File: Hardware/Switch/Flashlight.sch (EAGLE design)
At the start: 13 parts

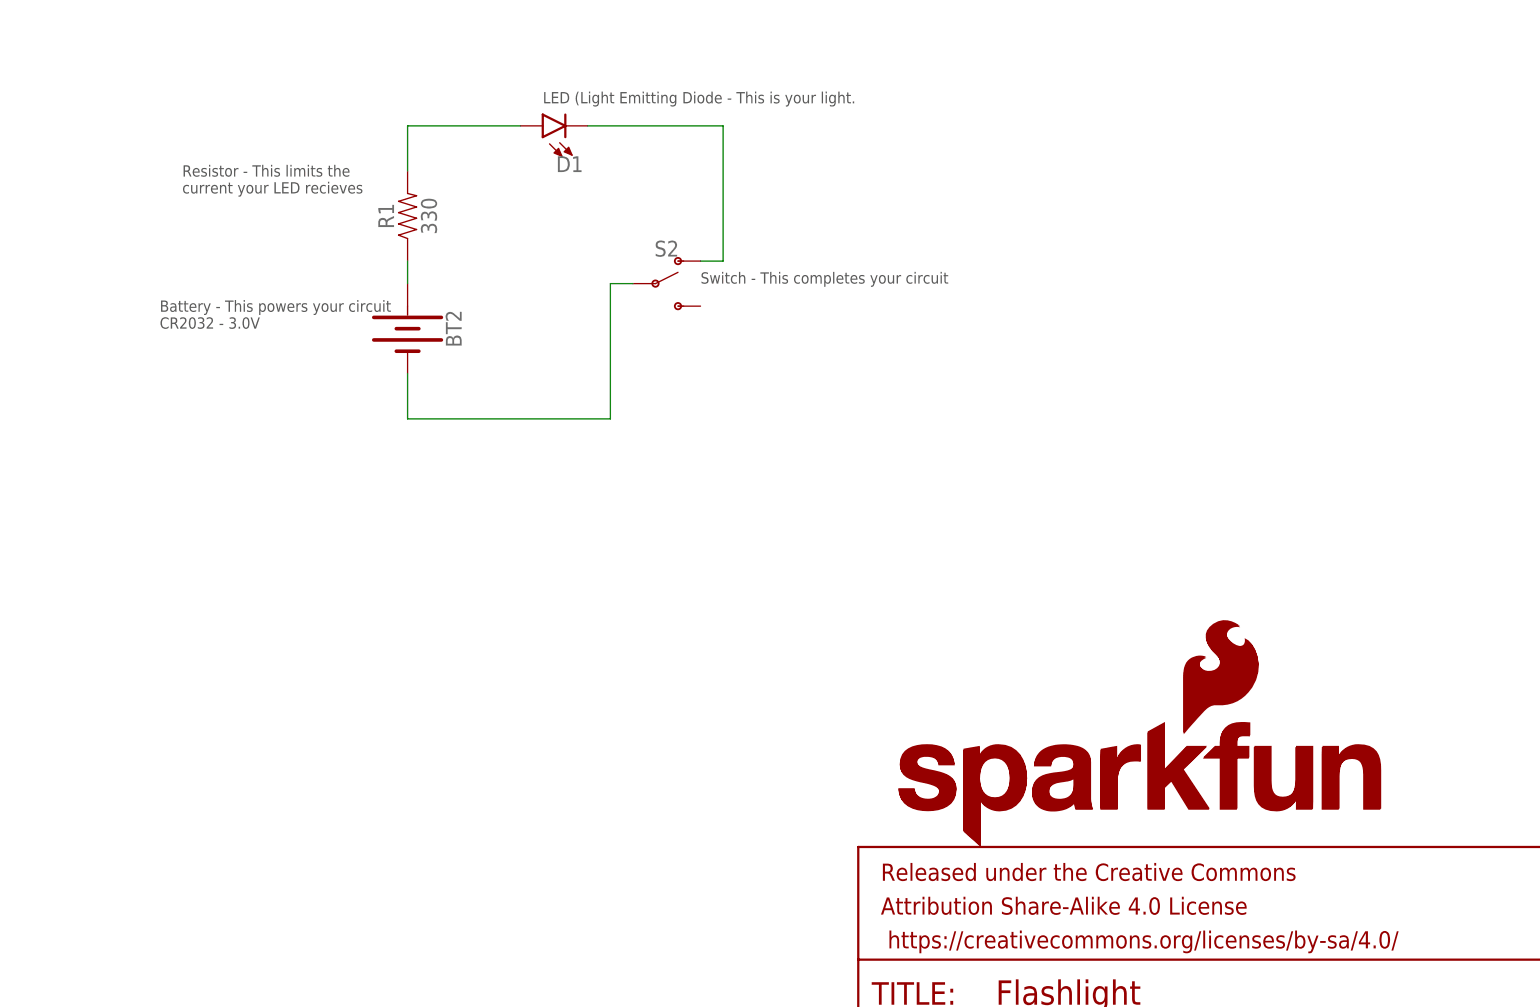
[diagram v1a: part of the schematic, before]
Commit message: Reds
Updated silk to be cleaner, updated version number
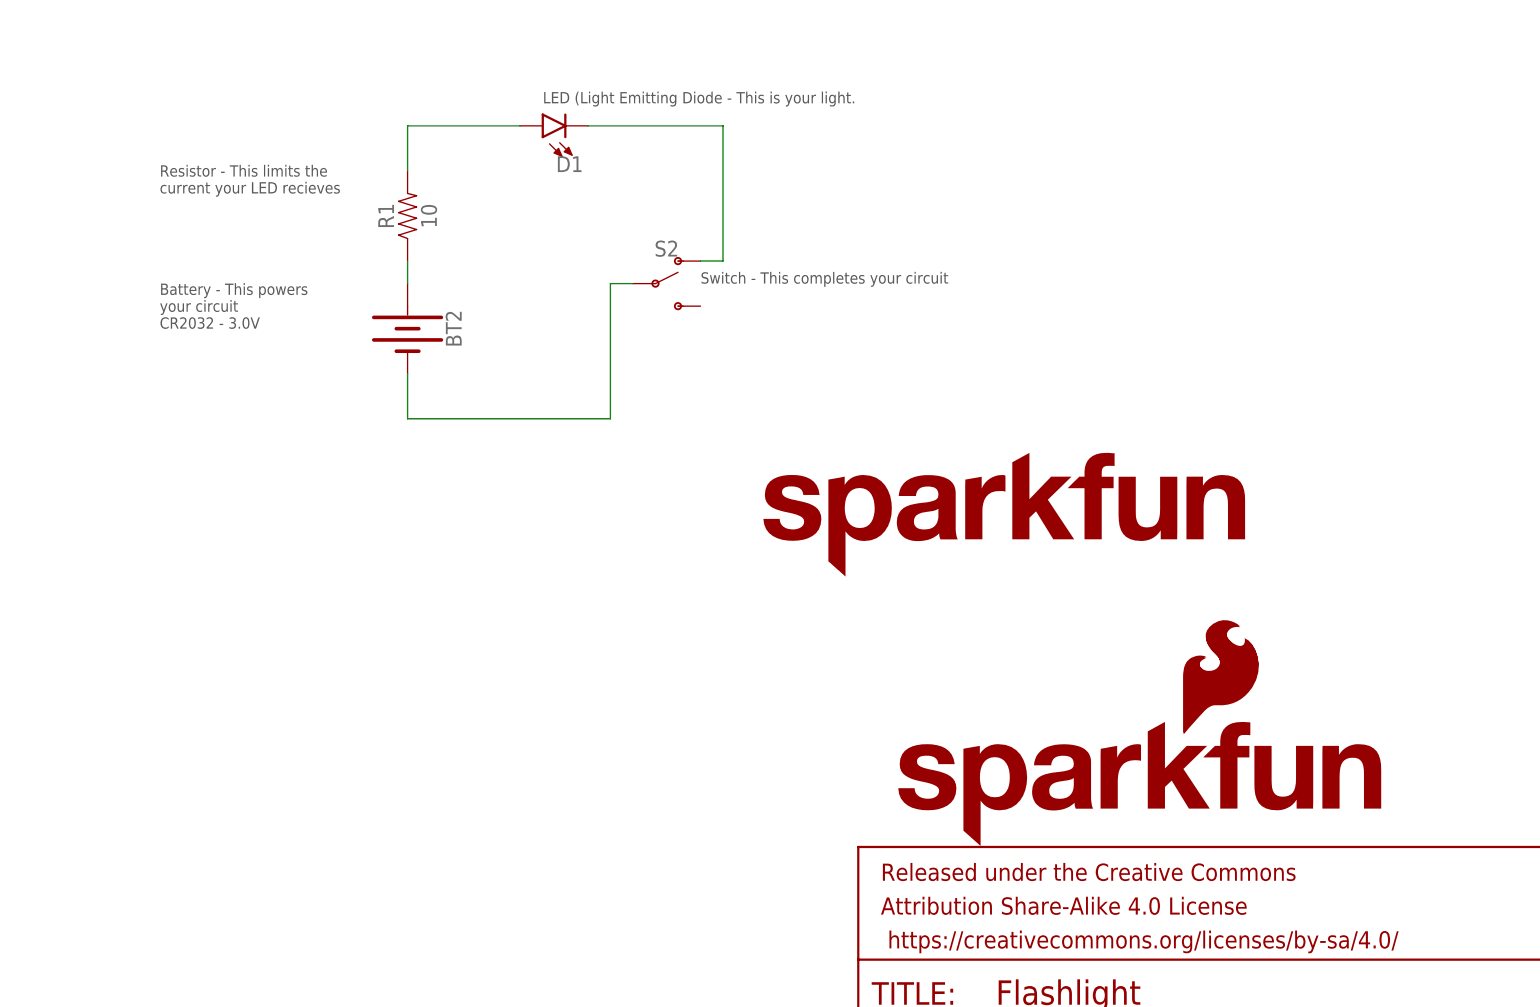
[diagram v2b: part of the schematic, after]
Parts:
- LOGO4: value SFE_LOGO_NAME.1_INCH -> SFE_LOGO_NAME.2_INCH; device SparkFun-Aesthetics:SFE_LOGO_NAME.1_INCH -> SparkFun-Aesthetics:SFE_LOGO_NAME.2_INCH
- R1: value 330 -> 10
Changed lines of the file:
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@@
 <attribute name="PROD_ID" value="9903"/>
 </part>
-<part name="R1" library="SparkFun-Resistors" deviceset="RESISTOR" device="AXIAL-0.3-KIT" value="330">
+<part name="R1" library="SparkFun-Resistors" deviceset="RESISTOR" device="AXIAL-0.3-KIT" value="10">
 <attribute name="PROD_ID" value="8371"/>
 </part>
@@
 <part name="H2" library="SparkFun-Hardware" deviceset="STAND-OFF" device=""/>
 <part name="S2" library="SparkFun-Switches" deviceset="SWITCH-SPDT" device="-PTH-11.6X4.0MM-KIT"/>
-<part name="LOGO4" library="SparkFun-Aesthetics" deviceset="SFE_LOGO_NAME" device=".1_INCH"/>
 <part name="LOGO3" library="SparkFun-Aesthetics" deviceset="SFE_LOGO_NAME_FLAME" device=".2_INCH"/>
 <part name="BT2" library="SparkFun-Batteries" deviceset="BATTERY" device="-20MM_PTH_KIT">
@@
 <part name="H3" library="SparkFun-Hardware" deviceset="STAND-OFF" device=""/>
 <part name="H4" library="SparkFun-Hardware" deviceset="STAND-OFF" device=""/>
+<part name="LOGO4" library="SparkFun-Aesthetics" deviceset="SFE_LOGO_NAME" device=".2_INCH"/>
 </parts>
 <sheets>
@@
 <text x="167.64" y="7.62" size="3.81" layer="94">Michelle Shorter</text>
 <text x="43.18" y="134.62" size="5.08" layer="97" font="vector">SparkFun Flashlight Soldering Kit</text>
-<text x="111.76" y="119.38" size="1.27" layer="97">LED (Light Emitting Diode - This is your light.</text>
-<text x="71.12" y="109.22" size="1.27" layer="97">Resistor - This limits the
+<text x="111.76" y="119.38" size="1.27" layer="97" font="vector">LED (Light Emitting Diode - This is your light.</text>
+<text x="68.58" y="109.22" size="1.27" layer="97" font="vector">Resistor - This limits the
 current your LED recieves</text>
-<text x="129.54" y="99.06" size="1.27" layer="97">Switch - This completes your circuit</text>
-<text x="68.58" y="93.98" size="1.27" layer="97">Battery - This powers your circuit
+<text x="129.54" y="99.06" size="1.27" layer="97" font="vector">Switch - This completes your circuit</text>
+<text x="68.58" y="93.98" size="1.27" layer="97" font="vector">Battery - This powers
+your circuit
 CR2032 - 3.0V</text>
 <text x="236.982" y="6.35" size="3.81" layer="94">v02</text>
@@
 <instance part="H2" gate="G$1" x="243.84" y="25.4"/>
 <instance part="S2" gate="1" x="124.46" y="99.06"/>
-<instance part="LOGO4" gate="G$1" x="149.86" y="35.56"/>
 <instance part="LOGO3" gate="G$1" x="151.13" y="35.306"/>
 <instance part="BT2" gate="G$1" x="96.52" y="93.98" rot="R270">
@@
 <instance part="H3" gate="G$1" x="236.22" y="30.48"/>
 <instance part="H4" gate="G$1" x="243.84" y="30.48"/>
+<instance part="LOGO4" gate="G$1" x="134.62" y="66.04"/>
 </instances>
 <busses>
